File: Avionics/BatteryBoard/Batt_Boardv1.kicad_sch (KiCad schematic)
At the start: 36 parts, among them J1 Conn_02x26_Odd_Even, J2 Conn_02x26_Odd_Even, Q1 IRF7458, Q2 IRF7458, U2 BQ29200DRBR

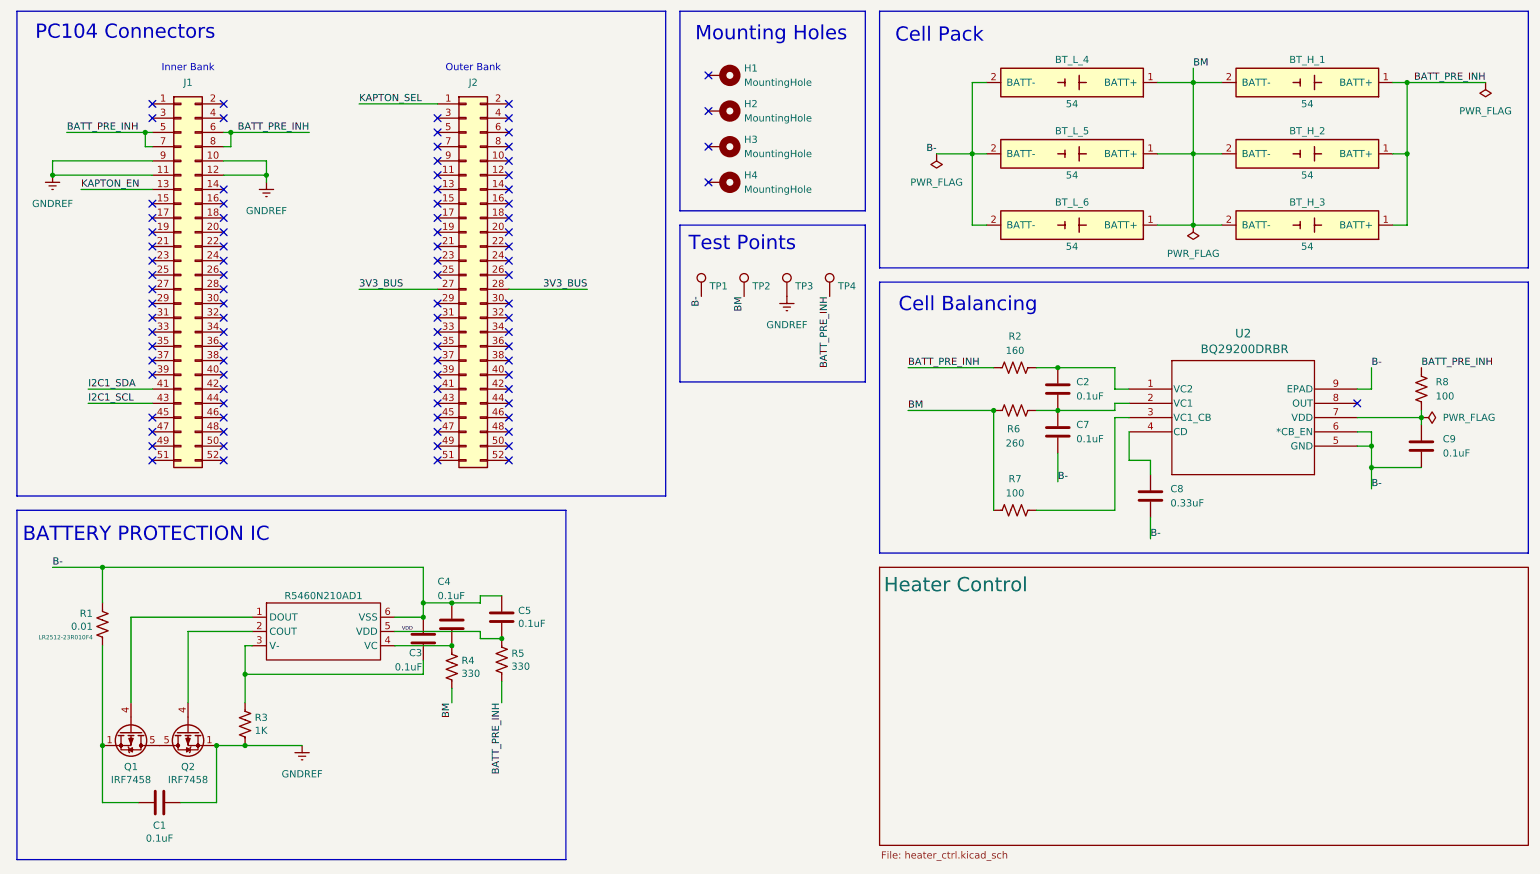
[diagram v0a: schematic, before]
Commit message: batt_brd: add temp sensors and adc ic
* Add 4x LM135 temperature sensors
* Add TLA2024 ADC to read sensors
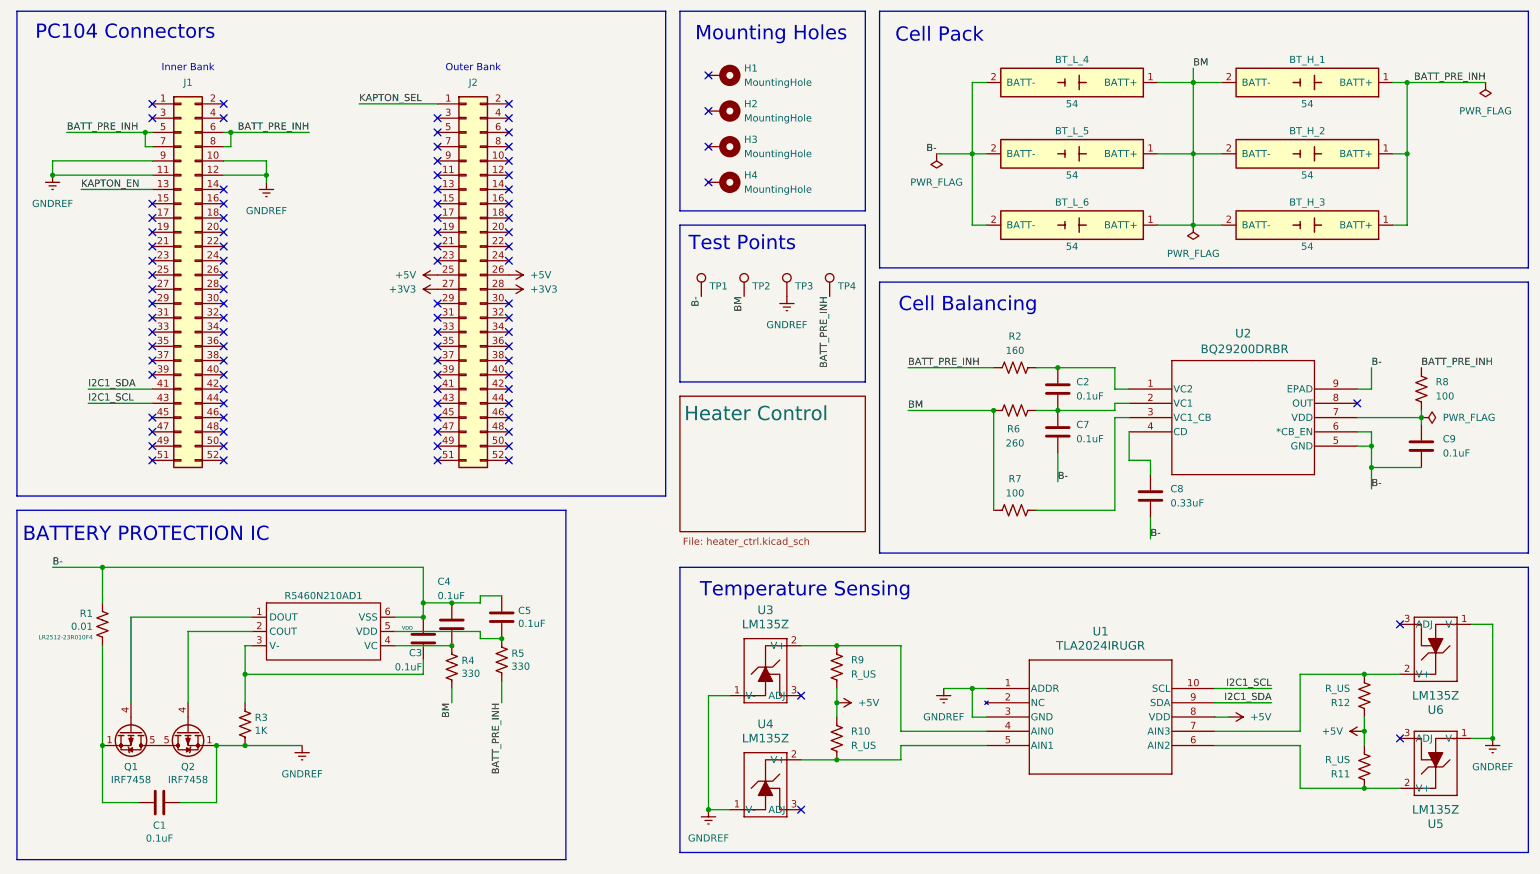
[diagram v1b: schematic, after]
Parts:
- added R10, R11, R12, R9: R_US, symbol Device:R_US
- added U1: TLA2024IRUGR, RUG10_TEX, symbol TLA2024IRUGR:TLA2024IRUGR
- added U3, U4, U5, U6: LM135Z, TO-226_STM, symbol LM135Z:LM135Z
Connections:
- net GNDREF: now also U1.1 (ADDR), U1.3 (GND), U3.1 (V-), U4.1 (V-), U5.1 (V-), U6.1 (V-)
- net I2C1_SCL: now also U1.10 (SCL)
- net I2C1_SDA: now also U1.9 (SDA)
- net +5V: now reaches J2.25 (Pin_25)
- net +5V: now also J2.26 (Pin_26), R10.2, R11.2, R12.1, R9.1, U1.8 (VDD)
- net 3V3_BUS renamed +3V3
- new net: R12.2, U1.7 (AIN3), U6.2 (V+)
- new net: R9.2, U1.4 (AIN0), U3.2 (V+)
- new net: R10.1, U1.5 (AIN1), U4.2 (V+)
- new net: R11.1, U1.6 (AIN2), U5.2 (V+)
- no-connect marks 95 -> 97
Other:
- note added: "Temperature Sensing"

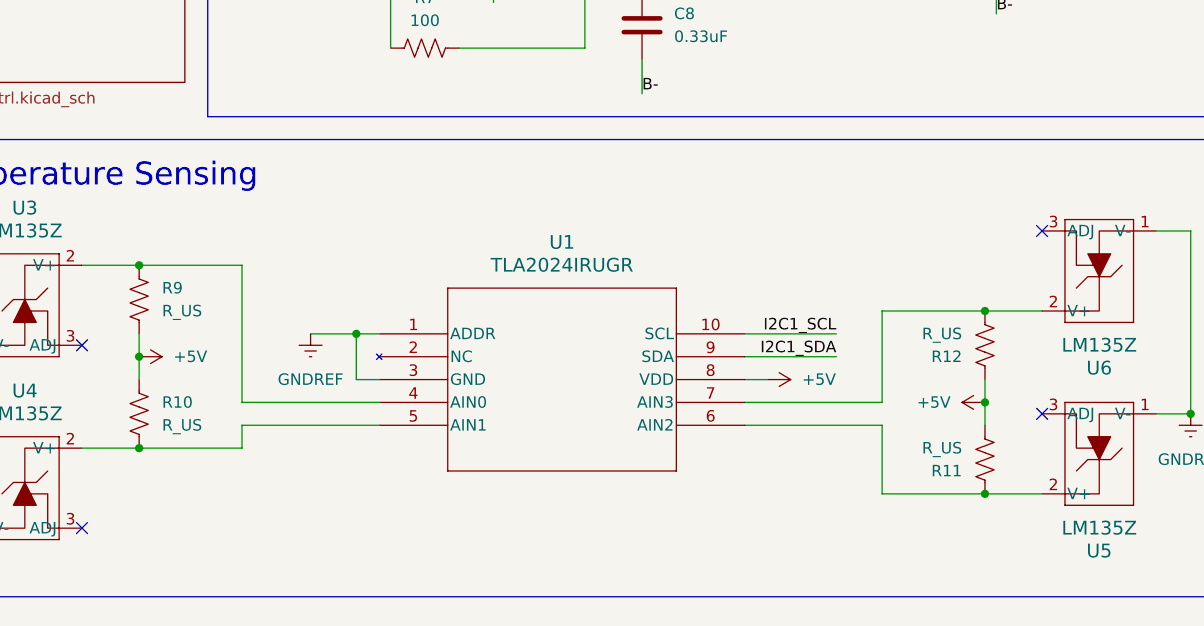
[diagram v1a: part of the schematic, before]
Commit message: batt_brd: add passive values for temp sensing
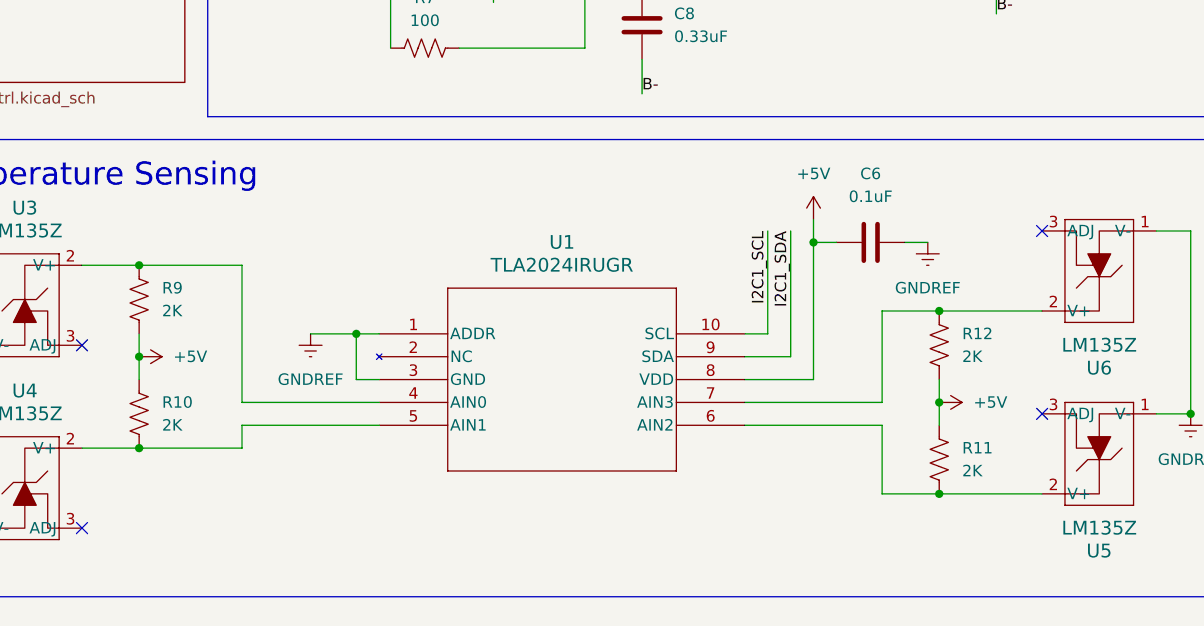
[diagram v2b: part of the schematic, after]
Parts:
- added C6: 0.1uF, symbol Device:C
- R10, R11, R12, R9: value R_US -> 2K
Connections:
- net +5V: now also C6.2
- net GNDREF: now also C6.1
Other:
- moved on the sheet: R11, R12

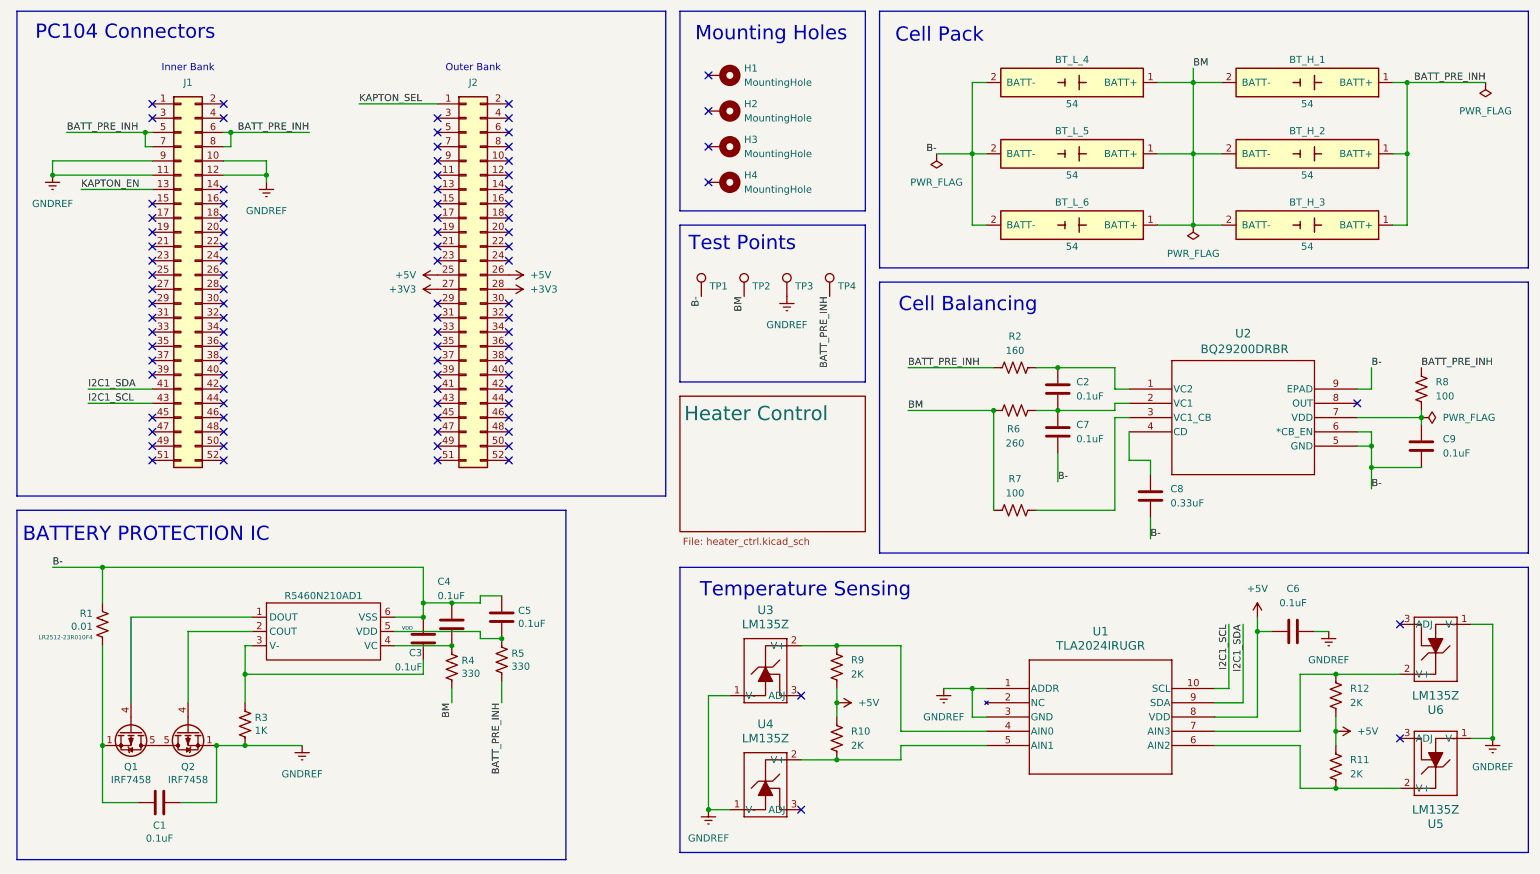
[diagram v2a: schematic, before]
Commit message: batt_brd: make R5460 lib in proj dir
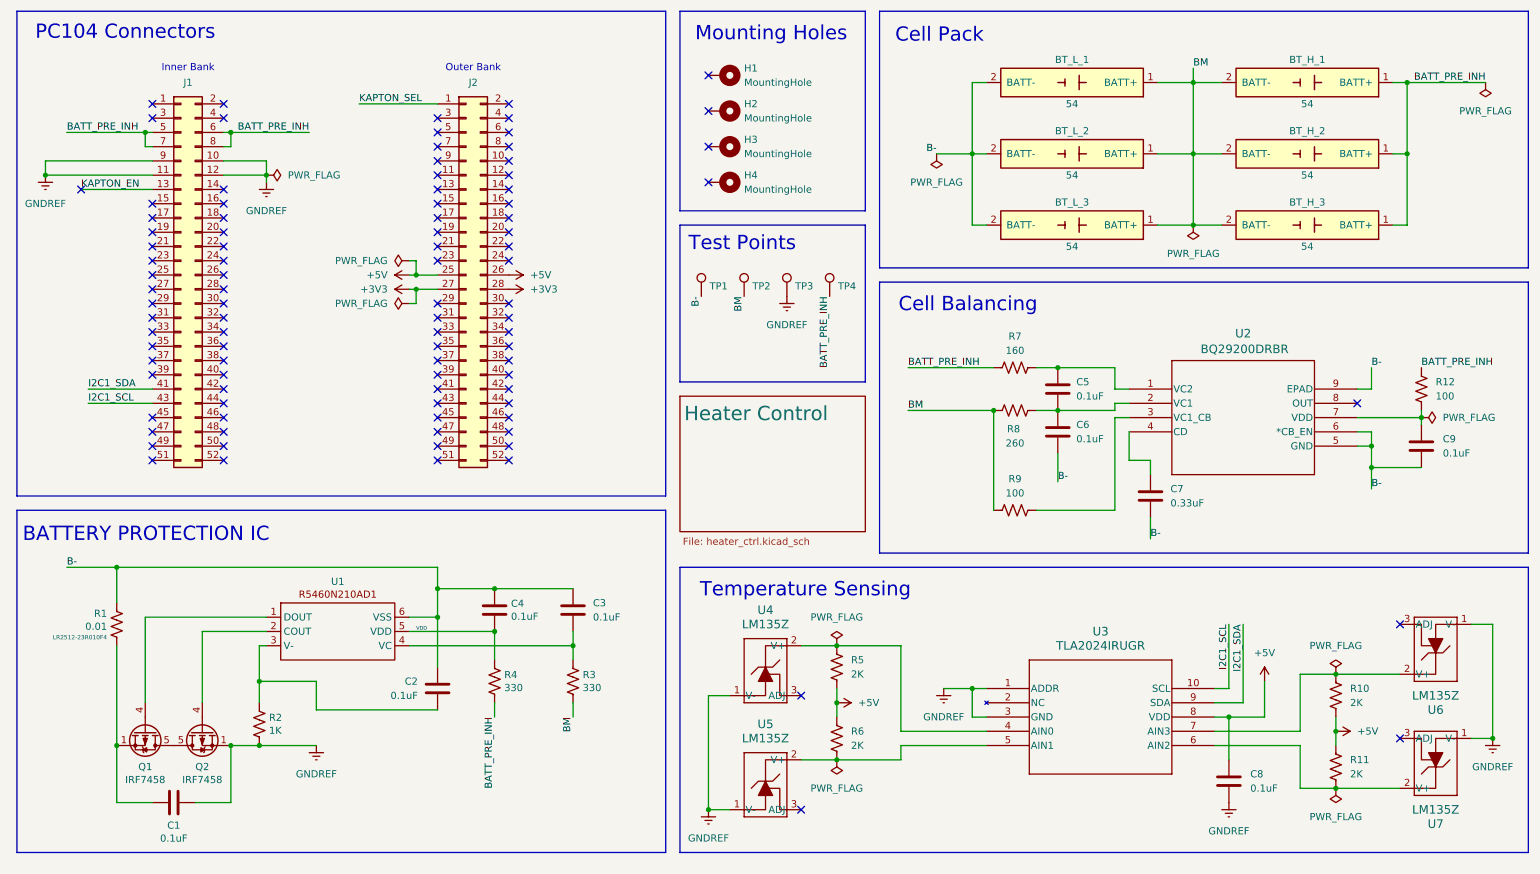
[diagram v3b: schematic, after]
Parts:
- U1: renamed from R5460N210AD1; symbol NewSymbols:R5460N233AF -> R5460:R5460N210AD1
- renumbered BT_L_4 to BT_L_1, BT_L_5 to BT_L_2, BT_L_6 to BT_L_3, C3 to C2, C4 to C3, C5 to C4, C2 to C5, C7 to C6, C8 to C7, C6 to C8, R12 to R10, R8 to R12, R3 to R2, R4 to R3, R5 to R4, R9 to R5, R10 to R6, R2 to R7, R6 to R8, R7 to R9, U1 to U3, U3 to U4, U4 to U5, U5 to U7
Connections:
- net +5V: now also C8.1; no longer C8.2
- net GNDREF: now also C8.2; no longer C8.1
- no-connect marks 97 -> 98
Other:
- moved on the sheet: C1, C2, C3, C4, C8, Q1, Q2, R1, R2, R3, R4

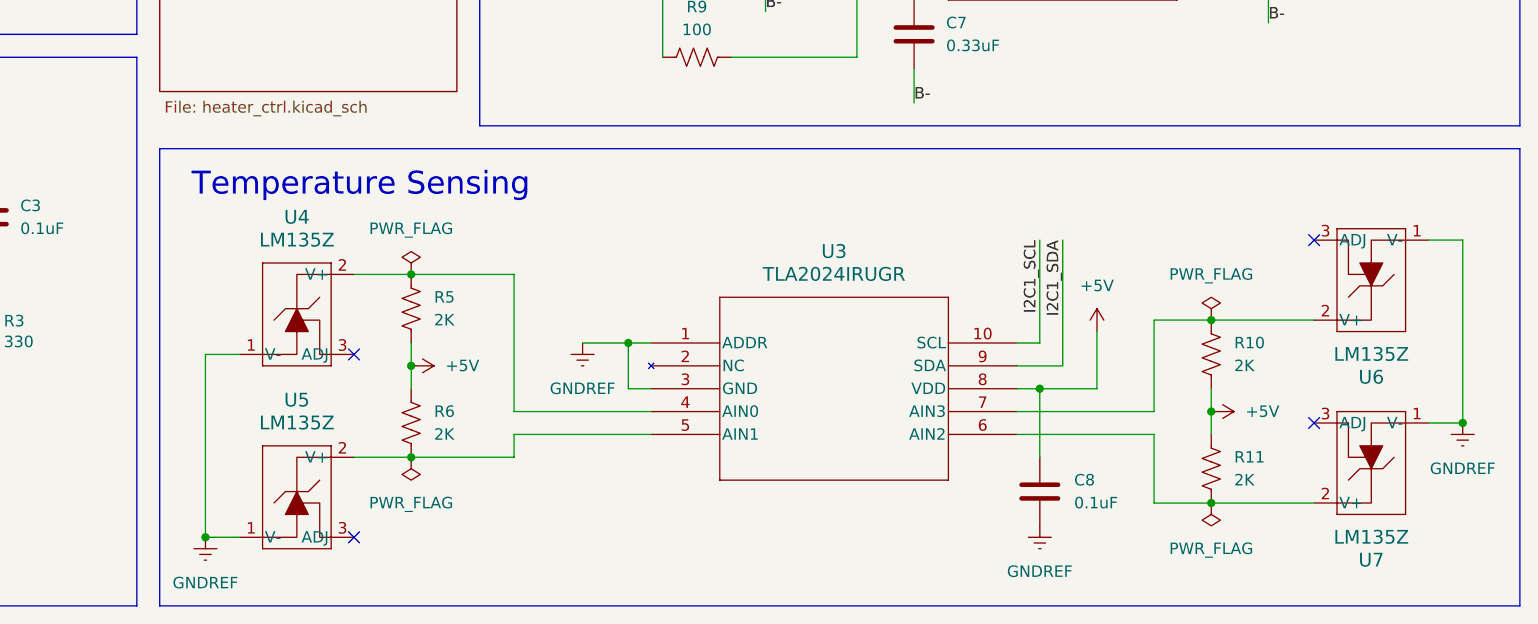
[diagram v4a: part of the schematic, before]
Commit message: batt_brd: switch to TMP/LM35s
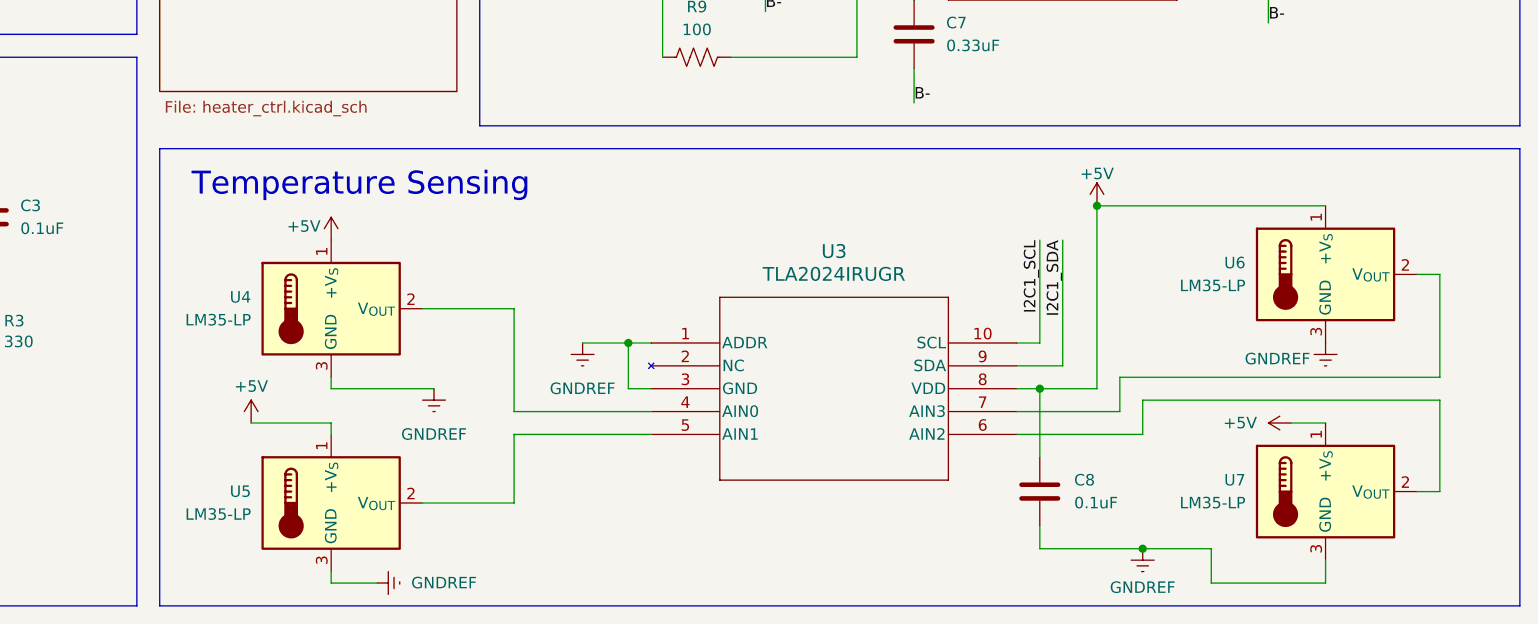
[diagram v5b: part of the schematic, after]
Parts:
- removed R10, R11, R5, R6: 2K, symbol Device:R_US
- removed U4, U5, U6, U7: LM135Z, TO-226_STM, symbol LM135Z:LM135Z
- added U4, U5, U6, U7: LM35-LP, Package_TO_SOT_THT:TO-92_Inline, symbol Sensor_Temperature:LM35-LP
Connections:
- net +5V: now also U4.1 (+V_{S}), U5.1 (+V_{S}), U6.1 (+V_{S}), U7.1 (+V_{S})
- net GNDREF: now also U4.3 (GND), U5.3 (GND), U6.3 (GND), U7.3 (GND)
- net at U3.7 (AIN3): now also U6.2 (V_{OUT})
- net at U3.4 (AIN0): now also U4.2 (V_{OUT})
- net at U3.5 (AIN1): now also U5.2 (V_{OUT})
- net at U3.6 (AIN2): now also U7.2 (V_{OUT})
- no-connect marks 98 -> 94
